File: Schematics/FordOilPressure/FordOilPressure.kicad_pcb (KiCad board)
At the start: 2 copper layers, 50 x 39 mm, 14 parts, among them J1 I/O Connector, J2 ISP Prog, J3 LCD Conn, Q1 PHB21N06LT,118, U1 ATtiny85-20S, U2 LM1085-5.0

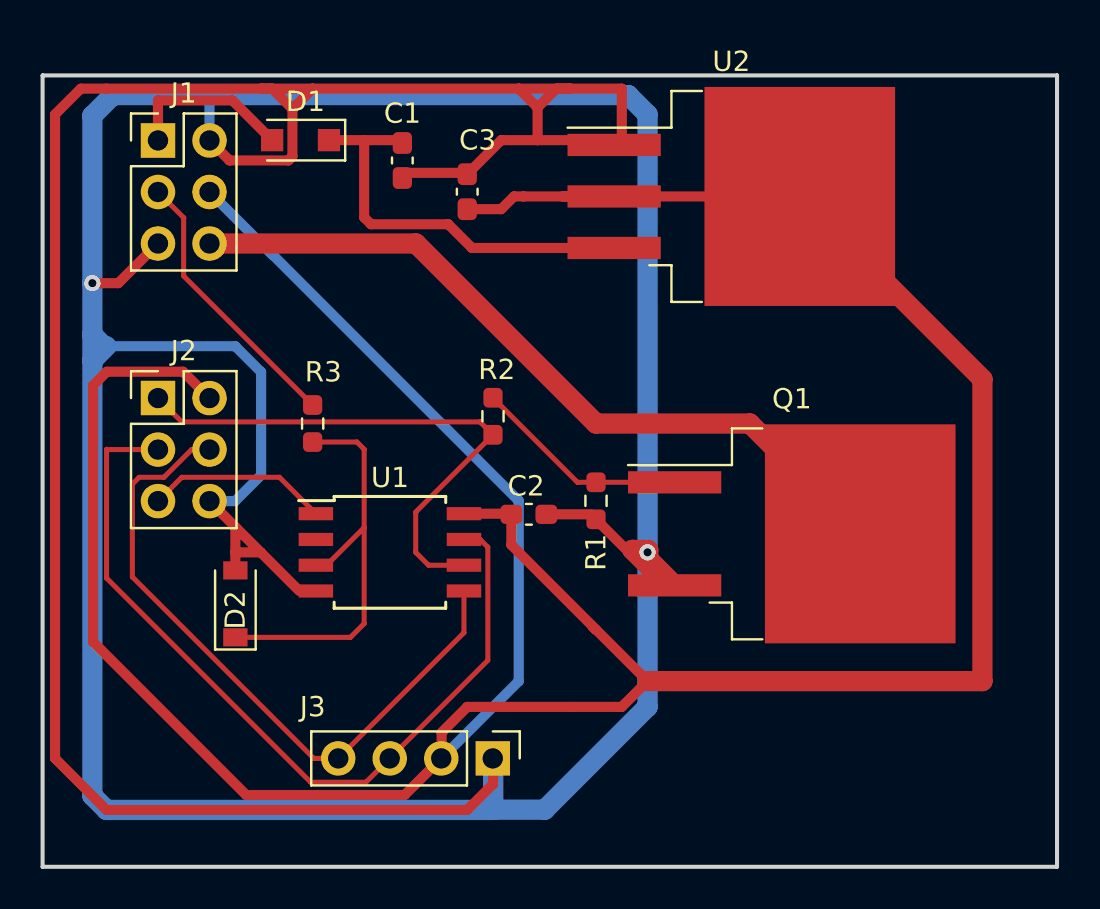
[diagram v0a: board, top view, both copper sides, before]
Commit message: This is the latest with ATTiny1626
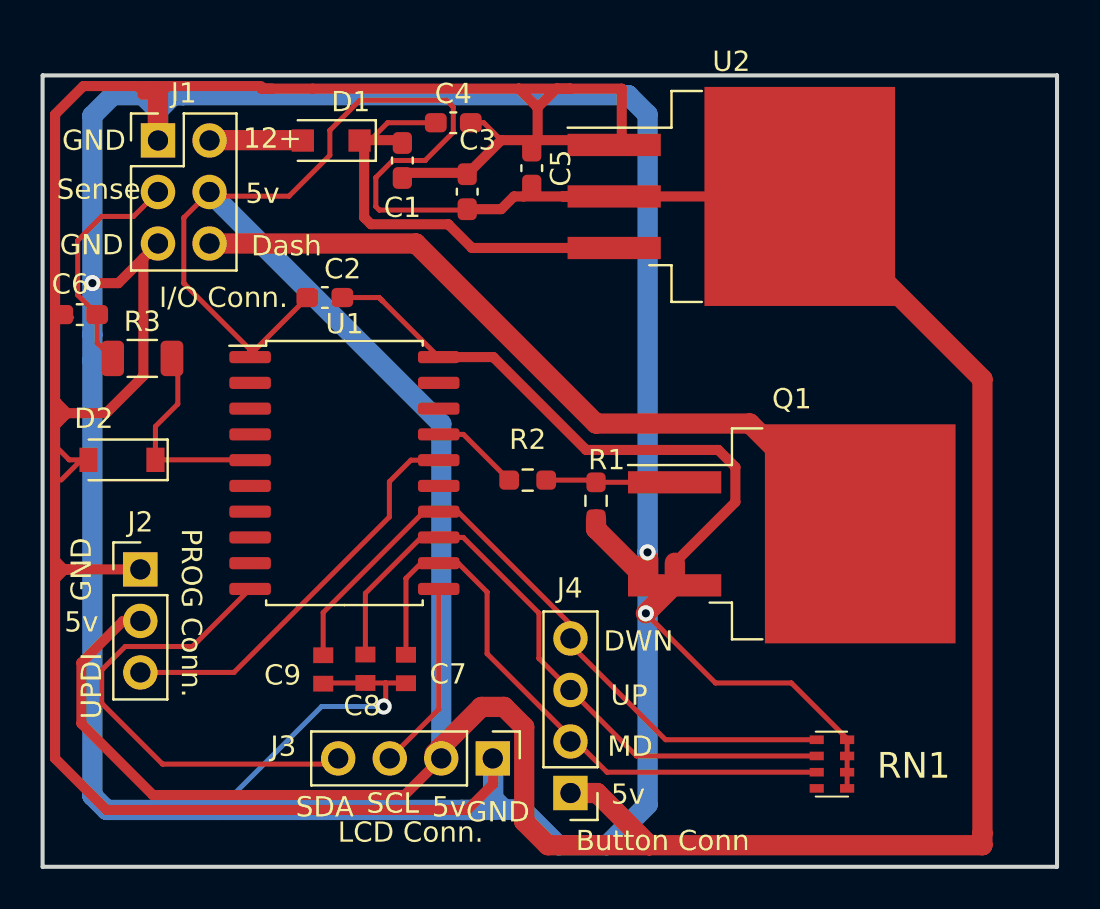
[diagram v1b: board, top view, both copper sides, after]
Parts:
- added C4: .1uF, Capacitor_SMD:C_0603_1608Metric_Pad1.08x0.95mm_HandSolder, F.Cu at (32.3, 14.4)
- added C5: 10uF, Capacitor_SMD:C_0603_1608Metric_Pad1.08x0.95mm_HandSolder, F.Cu at (36.2, 16.6)
- added C6: .33uF, Capacitor_SMD:C_0603_1608Metric_Pad1.08x0.95mm_HandSolder, F.Cu at (13.9, 23.8)
- added C7: 0603YC105KAT2A, SamacSys_Parts:CAPC1608X94N, F.Cu at (30.0, 41.3)
- added C8: 0603YC105KAT2A, SamacSys_Parts:CAPC1608X94N, F.Cu at (28.0, 41.3)
- added C9: 0603YC105KAT2A, SamacSys_Parts:CAPC1608X94N, F.Cu at (25.9, 41.3)
- added J4: Btn Connect, Connector_PinHeader_2.54mm:PinHeader_1x04_P2.54mm_Vertical, F.Cu at (38.1, 47.4)
- added RN1: EXBV8V683JV, SamacSys_Parts:EXBV8V101JV, F.Cu at (51.0, 46.0)
- C3: value 10uF -> .33uF
- J2: value ISP Prog -> UPDI; footprint Connector_PinHeader_2.54mm:PinHeader_2x03_P2.54mm_Vertical -> Connector_PinHeader_2.54mm:PinHeader_1x03_P2.54mm_Vertical
- R3: footprint Resistor_SMD:R_0603_1608Metric_Pad0.98x0.95mm_HandSolder -> Resistor_SMD:R_1206_3216Metric
- U1: value ATtiny85-20S -> ATtiny1616-S; footprint Package_SO:SOIC-8W_5.3x5.3mm_P1.27mm -> Package_SO:SOIC-20W_7.5x12.8mm_P1.27mm
- moved C2 14.7 mm to (26.0, 23.0)
- moved D2 9.04 mm to (16.0, 31.0), turned to 180 degrees
- moved R3 8.99 mm to (17.0, 26.0), turned to 0 degrees
- moved J2 8.49 mm to (16.9, 36.4)
- moved U1 4.51 mm to (27.0, 31.7)
- moved R2 3.58 mm to (36.0, 32.0), turned to 0 degrees
- moved D1 1.51 mm to (26.3, 15.3)
- turned C1 to 90 degrees
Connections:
- C1 pad 1: Net-(D1-Pad1) -> GND
- C1 pad 2: GND -> Net-(U2-Pad3)
- D1 pad 1: Net-(D1-Pad1) -> Net-(U2-Pad3)
- D2 pad 1: Net-(U1-Pad3) -> Net-(D2-Pad1)
- J1 pad 1: Net-(D1-Pad2) -> GND
- J1 pad 2: GND -> Net-(D1-Pad2)
- J2 pad 1: Net-(R2-Pad1) -> GND
- J2 pad 3: Net-(J3-Pad3) -> Net-(J2-Pad3)
- R3 pad 2: Net-(U1-Pad3) -> Net-(D2-Pad1)
- U1 pad 1: Net-(J2-Pad5) -> Net-(C2-Pad1)
- U1 pad 3: Net-(U1-Pad3) -> unconnected-(U1-Pad3)
- U1 pad 4: GND -> unconnected-(U1-Pad4)
- U1 pad 5: Net-(J3-Pad4) -> Net-(D2-Pad1)
- U1 pad 6: Net-(R2-Pad1) -> unconnected-(U1-Pad6)
- U1 pad 7: Net-(J3-Pad3) -> unconnected-(U1-Pad7)
- U1 pad 8: Net-(C2-Pad1) -> unconnected-(U1-Pad8)
- U2 pad 3: Net-(D1-Pad1) -> Net-(U2-Pad3)
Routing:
- net GND: track 285.9 -> 345.6 mm, vias 2 -> 4
- net Net-(U1-Pad14): track 0.00 -> 33.8 mm
- net Net-(U1-Pad13): track 0.00 -> 32.2 mm
- net Net-(J3-Pad3): track 41.3 -> 9.36 mm
- net Net-(U1-Pad12): track 0.00 -> 30.6 mm
- net Net-(C2-Pad1): track 163.0 -> 192.6 mm
- net Net-(R2-Pad1): track 27.3 -> 4.41 mm
- net Net-(U2-Pad3): track 0.00 -> 22.1 mm
- net Net-(U1-Pad3): track 21.1 -> 0.00 mm
- net Net-(D1-Pad1): track 20.2 -> 0.00 mm
- net Net-(J2-Pad3): track 0.00 -> 20.1 mm
- net Net-(J3-Pad4): track 33.8 -> 22.9 mm
- net Net-(D2-Pad1): track 0.00 -> 10.2 mm
- net Net-(J2-Pad5): track 9.01 -> 0.00 mm
- net Net-(Q1-Pad1): track 10.7 -> 6.73 mm
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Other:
- board text added: "12+"
- board text added: "5v"
- board text added: "AMPED Oil Pressure V 1.1 alshowto.com"
- board text added: "Button Conn"
- board text added: "DWN"
- board text added: "Dash"
- board text added: "GND"
- board text added: "I/O Conn."
- board text added: "LCD Conn."
- board text added: "MD"
- board text added: "PROG Conn."
- board text added: "SCL"
- board text added: "SDA"
- board text added: "Sense"
- board text added: "UP"
- board text added: "UPDI"
- board text removed: "AMPED Oil Pressure V 1.0 alshowto.com"
